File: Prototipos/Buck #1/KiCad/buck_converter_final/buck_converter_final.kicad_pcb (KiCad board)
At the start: 2 copper layers, 50 x 100 mm, 52 parts, among them J2 Screw_Terminal_01x02, J3 Screw_Terminal_01x02, K1 SANYOU_SRD_Form_C, M5_BotL MountingHole_5.3mm_M5, M5_BotR MountingHole_5.3mm_M5, M5_TopL MountingHole_5.3mm_M5, M5_TopR MountingHole_5.3mm_M5, Q1 NPN, Q2 IRF9540NPBF, Q3 BC548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

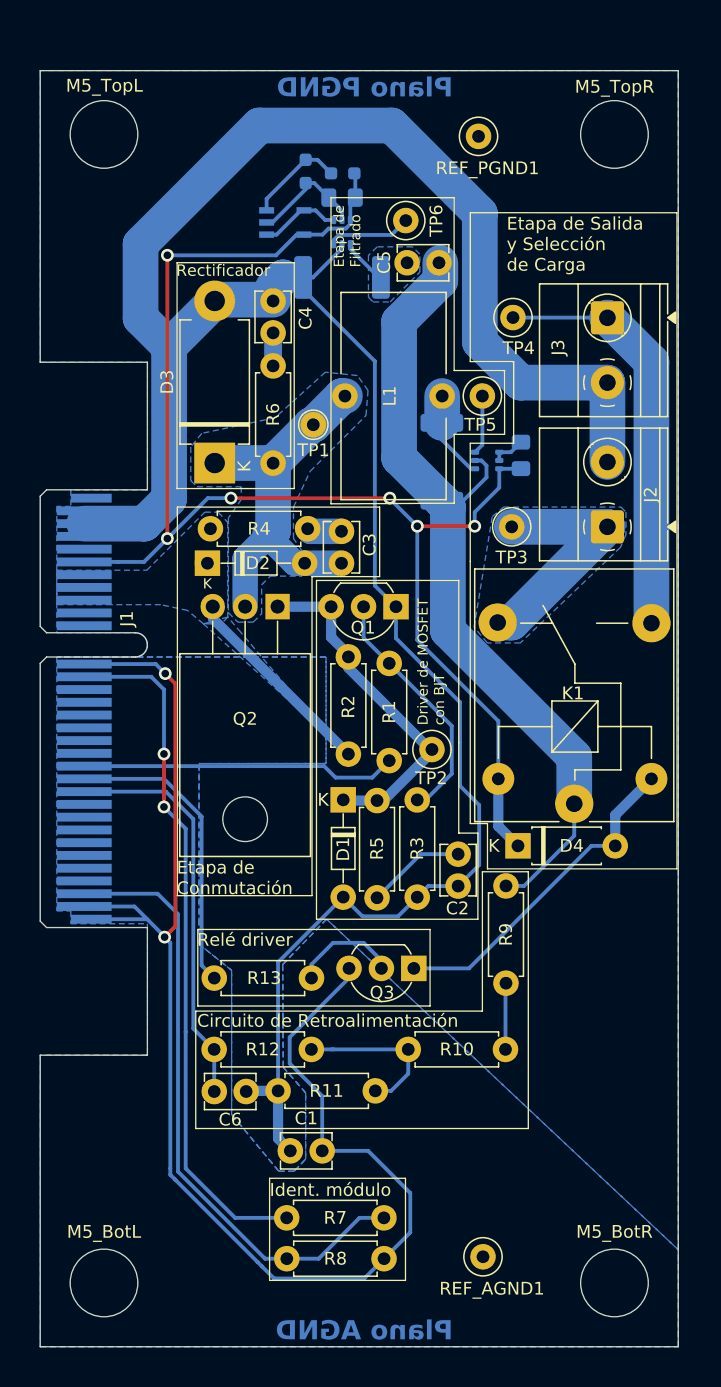
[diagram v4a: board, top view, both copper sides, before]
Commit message: Comenzar rediseño placa Buck
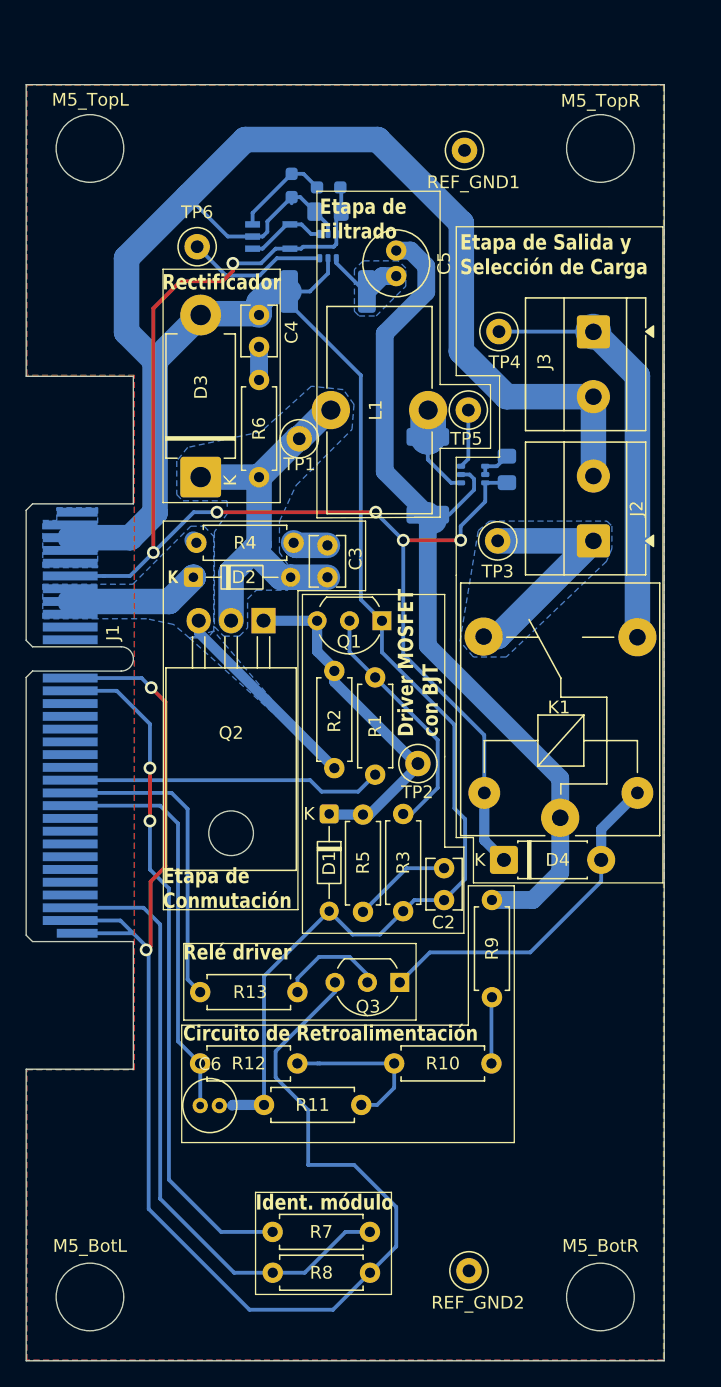
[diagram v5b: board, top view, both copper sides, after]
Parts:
- removed C1: 1u, Capacitor_THT:C_Disc_D3.8mm_W2.6mm_P2.50mm
- removed REF_AGND1: AGND, TestPoint:TestPoint_Loop_D1.80mm_Drill1.0mm_Beaded
- removed REF_PGND1: PGND, TestPoint:TestPoint_Loop_D1.80mm_Drill1.0mm_Beaded
- added REF_GND1: GND, TestPoint:TestPoint_Loop_D1.80mm_Drill1.0mm_Beaded, F.Cu at (138.1, 39.2)
- added REF_GND2: GND, TestPoint:TestPoint_Loop_D1.80mm_Drill1.0mm_Beaded, F.Cu at (138.4, 127.0)
- C5: value 42u -> 47u; footprint Capacitor_THT:C_Disc_D3.8mm_W2.6mm_P2.50mm -> Capacitor_THT:C_Radial_D5.0mm_H11.0mm_P2.00mm
- C6: footprint Capacitor_THT:C_Disc_D3.8mm_W2.6mm_P2.50mm -> Capacitor_THT:C_Radial_D4.0mm_H7.0mm_P1.50mm
- D1, D2: value D_Schottky -> 1N5819
- D3: value D_Schottky -> SR560
- D4: value D_Small -> 1N4007
- moved TP6 16.5 mm to (117.1, 46.8)
- moved C5 3.48 mm to (132.7, 47.1), turned to -90 degrees
- moved Q3 1.56 mm to (133.0, 104.5)
- moved M5_TopR 1.56 mm to (148.7, 39.1)
- moved C2 1.56 mm to (136.4, 95.5)
- moved D4 1.56 mm to (141.1, 94.8)
- moved M5_BotR 1.56 mm to (148.7, 129.1)
- moved R9 1.56 mm to (140.2, 98.0)
- moved L1 1.56 mm to (127.6, 59.6)
- moved TP1 1.56 mm to (125.1, 61.9)
- moved U2 1.56 mm to (127.4, 46.8)
- moved U4 1.56 mm to (122.9, 46.0)
- moved C3 1.56 mm to (127.3, 70.2)
- moved C8 1.56 mm to (127.4, 44.0)
- moved D1 1.56 mm to (127.4, 91.2)
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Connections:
- C2 pad 2: PGND -> GND
- C4 pad 2: PGND -> GND
- C6 pad 2: PGND -> GND
- C7 pad 2: PGND -> GND
- C8 pad 2: PGND -> GND
- D1 pad 2: PGND -> GND
- D3 pad 2: PGND -> GND
- J1 pad 1: PGND -> GND
- J1 pad 2: PGND -> GND
- J1 pad 26: AGND -> GND
- J1 pad 7: AGND -> GND
- J2 pad 2: PGND -> GND
- J3 pad 2: PGND -> GND
- Q1 pad 1: PGND -> GND
- Q3 pad 3: AGND -> GND
- R11 pad 2: PGND -> GND
- R15 pad 1: PGND -> GND
- R17 pad 1: PGND -> GND
- R3 pad 2: PGND -> GND
- R8 pad 2: AGND -> GND
- U1 pad 1: PGND -> GND
- U1 pad 2: PGND -> GND
- U2 pad 2: PGND -> GND
- U2 pad 5: PGND -> GND
- U4 pad 2: PGND -> GND
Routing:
- net GND: track 0.00 -> 324.6 mm, vias 0 -> 2
- net PGND: track 205.7 -> 0.00 mm
- net AGND: track 110.8 -> 0.00 mm, vias 2 -> 0
- net 12V: track 16.0 -> 26.4 mm
- net Net-(TP6-Pad1): track 6.60 -> 11.1 mm
- net I_CURRENT_-: track 65.1 -> 69.1 mm
- net C_CURRENT_+: track 3.70 -> 6.50 mm
- net 5Vdc: track 110.6 -> 109.5 mm
- net UC_RELAY: track 23.5 -> 24.5 mm
- net RELAY_T2: track 26.2 -> 27.2 mm
- net 3.3Vcc: track 54.4 -> 53.5 mm
- net IDENT_V: track 48.5 -> 49.3 mm
- added copper zone on B.Cu, net GND
- added copper zone on F.Cu, net GND
- removed copper zone on B.Cu, net AGND
- removed copper zone on B.Cu, net PGND
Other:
- outline, holes or cut-outs redrawn
- board text added: "Driver MOSFET con BJT"
- board text removed: "Driver de MOSFET con BJT"
- board text removed: "Plano AGND"
- board text removed: "Plano PGND"

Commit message: Corrección para JLCPCB módulo buck
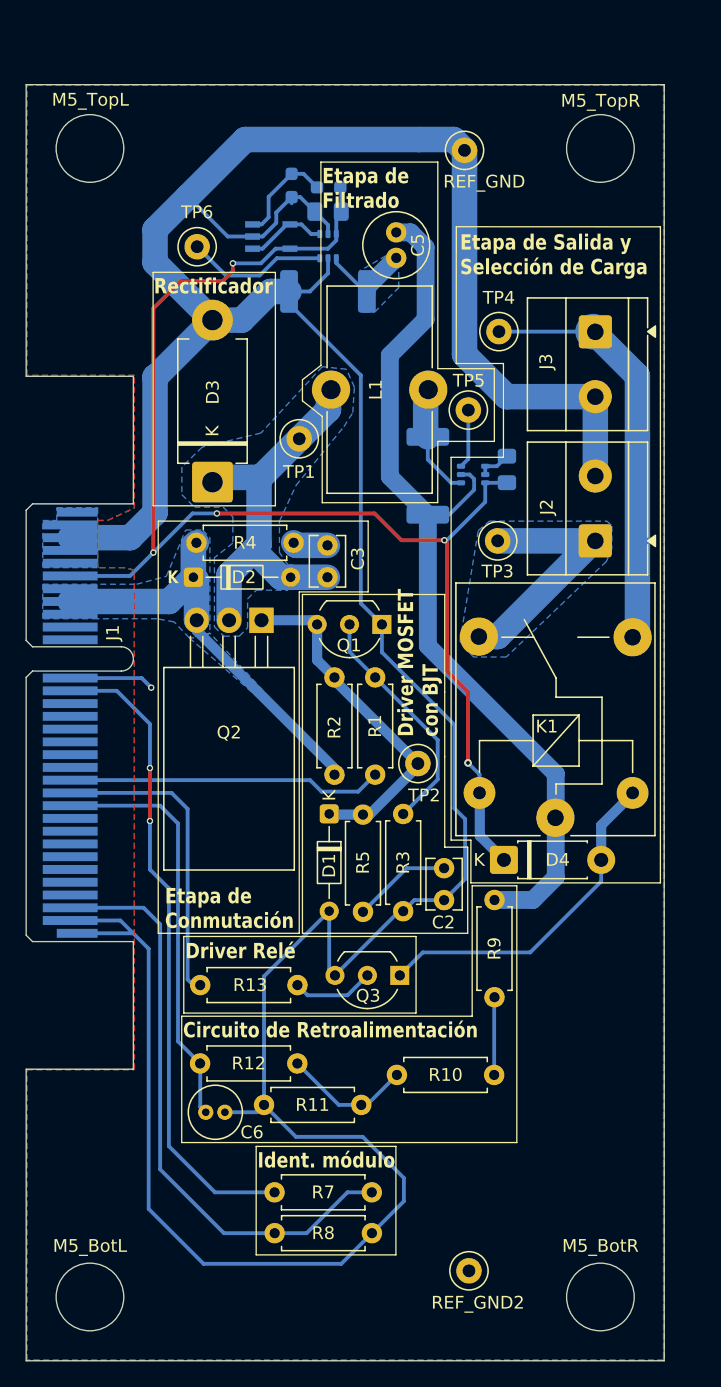
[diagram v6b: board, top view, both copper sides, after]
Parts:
- removed C4: ~, Capacitor_THT:C_Disc_D3.8mm_W2.6mm_P2.50mm
- removed R6: ~, Resistor_THT:R_Axial_DIN0207_L6.3mm_D2.5mm_P7.62mm_Horizontal
- moved R8 3.10 mm to (123.2, 124.1)
- moved R7 3.10 mm to (123.2, 120.9)
- moved L1 1.60 mm to (127.6, 58.0)
- moved C5 1.43 mm to (132.7, 45.7)
- moved D3 1.01 mm to (118.3, 65.2)
- moved R10 0.93 mm to (140.4, 111.7)
- moved C6 0.68 mm to (117.8, 114.6)
- moved Q3 0.55 mm to (133.0, 103.9)
- moved R13 0.55 mm to (117.3, 104.7)
- moved R2 0.51 mm to (127.9, 88.2)
- moved K1 0.38 mm to (145.2, 91.5)
- moved Q1 0.29 mm to (131.6, 76.4)
- moved R9 0.20 mm to (140.4, 98.0)
- moved Q2 0.16 mm to (122.1, 76.1)
- moved J2 0.15 mm to (148.3, 69.8)
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- renumbered REF_GND1 to REF_GND
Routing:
- net GND: track 324.6 -> 293.6 mm, vias 2 -> 1
- net 12V: track 26.4 -> 33.0 mm
- net 3.3Vcc: track 53.5 -> 50.8 mm
- net Net-(C4-Pad1): track 2.59 -> 0.00 mm
- net Net-(R10-Pad2): track 12.6 -> 10.1 mm
- net IDENT_V: track 49.3 -> 46.8 mm
- net 5Vdc: track 109.5 -> 107.2 mm, vias 6 -> 5
- net Net-(Q3-B): track 8.44 -> 6.46 mm
- net I_CURRENT_+: track 7.24 -> 8.98 mm
- net Net-(R10-Pad1): track 5.21 -> 6.10 mm
- net C_CURRENT_+: track 6.50 -> 7.28 mm
- net Net-(D2-A): track 31.3 -> 32.1 mm
- net RETRO_MICRO: track 31.9 -> 32.6 mm
- net Net-(Q1-B): track 20.4 -> 19.8 mm
- net RESISTIVE_LOAD: track 19.2 -> 19.7 mm
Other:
- board text added: "Driver Relé"
- board text removed: "Relé driver"

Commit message: Correcciones varias
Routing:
- net GND: track 293.6 -> 292.4 mm, vias 1 -> 139
- net I_CURRENT_-: track 69.0 -> 69.6 mm

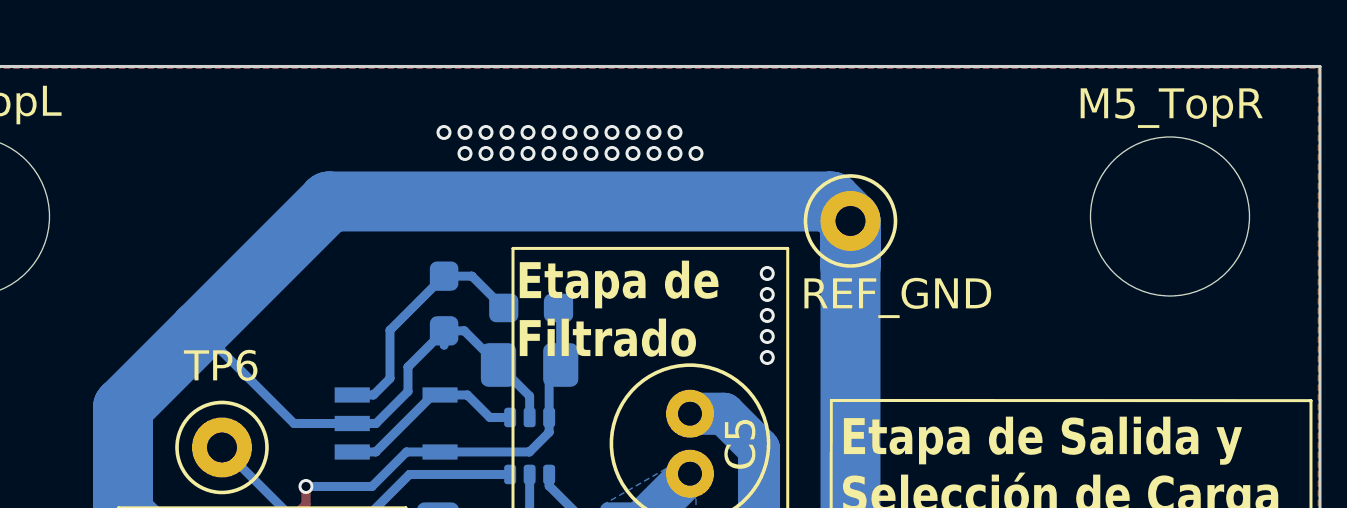
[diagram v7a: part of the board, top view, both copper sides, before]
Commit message: Agregar titulo de módulo y firma
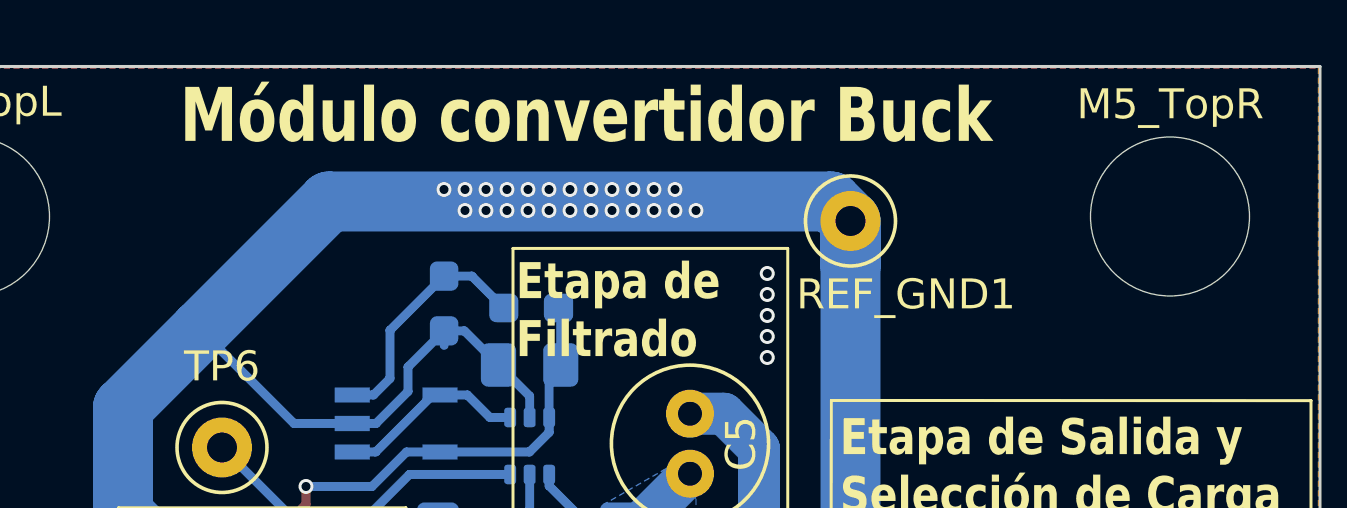
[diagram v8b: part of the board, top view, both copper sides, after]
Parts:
- renumbered REF_GND to REF_GND1
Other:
- board text added: "Módulo convertidor Buck"
- board text added: "NSH Designs"
